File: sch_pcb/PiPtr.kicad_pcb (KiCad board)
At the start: 4 copper layers, 105 x 141.9 mm, 327 parts, among them J101 GLOBAL LINK 1 LEFT, J102 GLOBAL LINK 1 RIGHT, J104 GLOBAL LINK 2 LEFT, J106 GLOBAL LINK 2 RIGHT, J107 RASPBERRY_PI, J111 FP_PIXEL, J112 AM2302, J113 I2C1_5V, J114 I2C0_3v3, J117 OLED, J201 TO_SOUNDCARD, J202 FROM_SOUNDCARD, J203 Radio Port, J204 DB9_FEMALE, J301 SPARE, J302 SPARE, J303 SPARE, J304 SPARE, J305 USER_GPIO_2, J306 SPARE, J307 SPARE, J308 USER_GPIO_1, J309 SPARE, J310 SPARE, J311 USER_ADC, J313 SPARE, J314 SPARE, J315 12VDC_IN, J401 TO_SOUNDCARD, J402 FROM_SOUNDCARD, J403 Radio Port, J404 DB9_FEMALE, Q101 2N7000, Q102 2N7000, Q103 2N7000, Q104 2N7000, Q105 2N7000, Q201 2N7000, Q202 2N7000, Q203 2N7000, Q301 SPARE, Q302 SPARE, Q401 2N7000, Q402 2N7000, Q403 2N7000, U101 MCP23017, U102 IP4234CZ6, U103 MCP4351, U104 74HC138, U105 74LV1T125, U106 MCP4351, U107 MCP4351, U108 IP4234CZ6, U109 IP4234CZ6, U110 CD4050B, U111 74LV1T125, U112 74LV1T125, U201 MCP6004N, U202 74LVC1G3157, U203 74LVC1G3157, U204 74LVC4066, U205 MCP6004N, U206 74LVC1G3157, U207 MCP6S26, U301 MCP23017, U302 SPARE, U303 SPARE, U304 MCP3008, U305 MCP1703A-2502/MB, U306 TPS54302, U401 MCP6004N, U402 74LVC1G3157, U403 74LVC1G3157, U404 74LVC4066, U405 MCP6004N, U406 74LVC1G3157, U407 MCP6S26

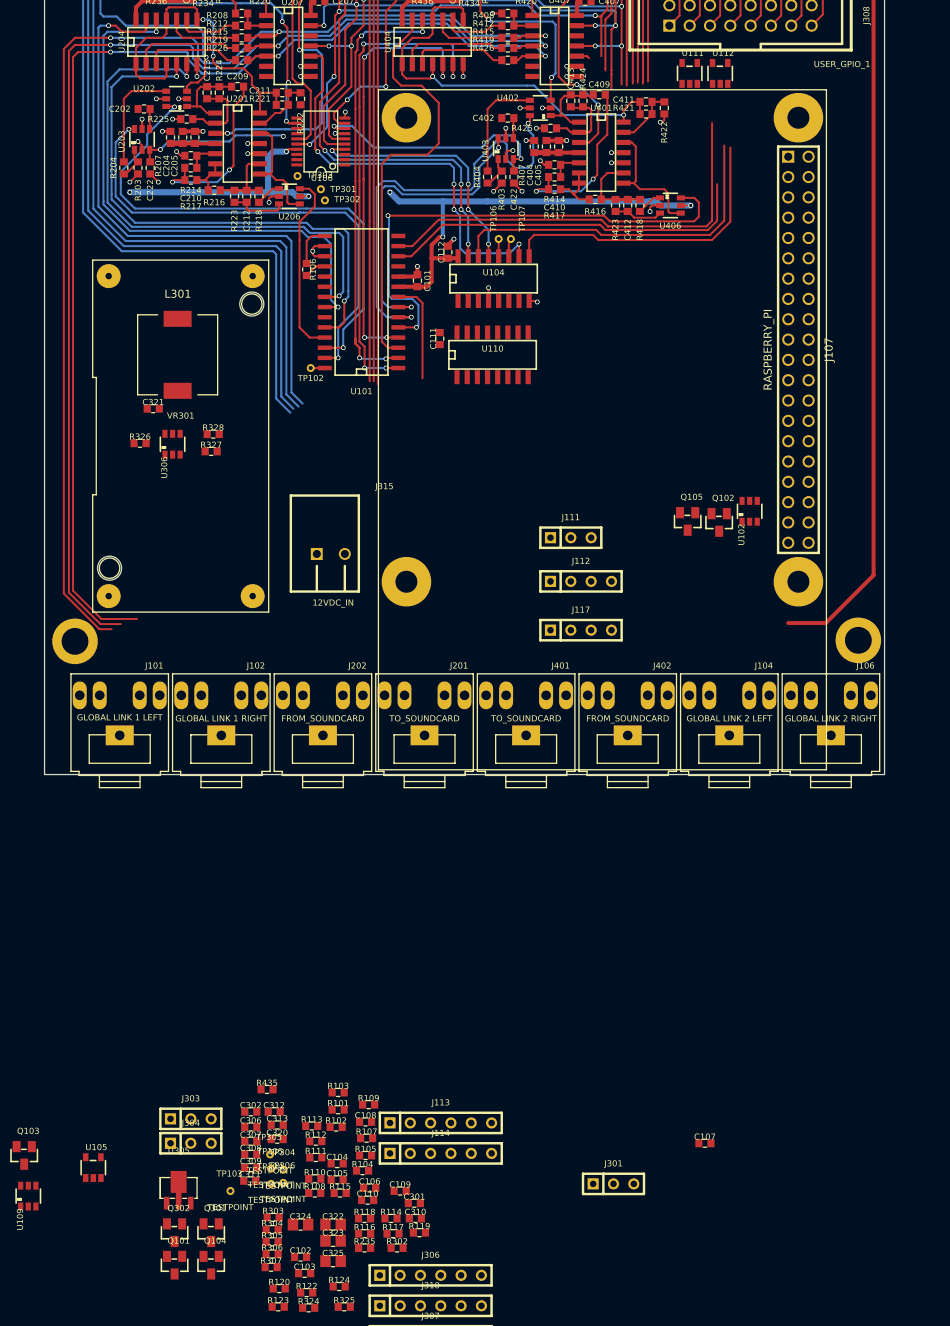
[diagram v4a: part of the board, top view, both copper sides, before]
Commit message: Add files via upload
Change link connectors to use a daughterboard for the off-rack links and 100mil headers for between-board links
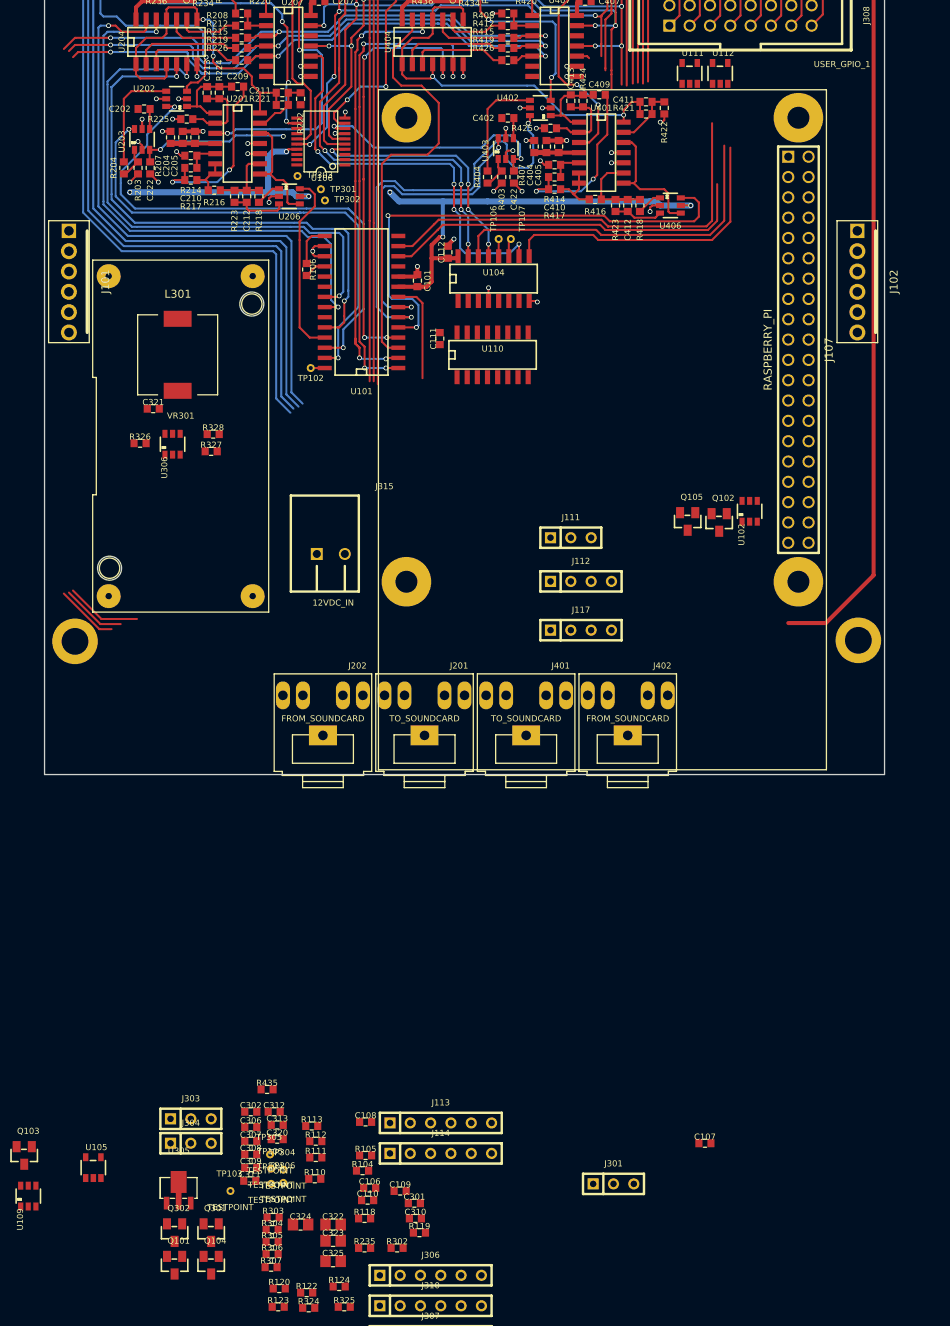
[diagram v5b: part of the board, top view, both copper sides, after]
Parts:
- removed C102, C104: 4.7u, lib:smd0603
- removed C103, C105: 0.1u, lib:smd0603
- removed J104: GLOBAL LINK 2 LEFT, lib:TRS3.5_5
- removed J106: GLOBAL LINK 2 RIGHT, lib:TRS3.5_5
- removed R101, R108: 100, lib:smd0603
- removed R102, R103, R107, R109, R114, R115, R116, R117: 2k, lib:smd0603
- C202, C402: value 4.7u -> 10u
- J101: value GLOBAL LINK 1 LEFT -> GLOBAL_LINK_LEFT; footprint lib:TRS3.5_5 -> lib:Molex_22-27-2061_100mil_6pin_verical
- J102: value GLOBAL LINK 1 RIGHT -> GLOBAL_LINK_RIGHT; footprint lib:TRS3.5_5 -> lib:Molex_22-27-2061_100mil_6pin_verical
- moved J102 96.7 mm to (158.8, 108.2), turned to 270 degrees
- moved J101 55.5 mm to (60.2, 108.2), turned to 270 degrees
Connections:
- J101 pad 1: GND -> +3V3
- J101 pad 2: /LINK1C -> /LINK1_AUD
- J101 pad 3: /LINK1_AUD -> /LINK1C
- J101 pad 4: Net-(J101-Pad4) -> GND
- J101 pad 5: Net-(J101-Pad5) -> /LINK2_AUD
- J102 pad 1: GND -> +3V3
- J102 pad 2: /LINK1C -> /LINK1_AUD
- J102 pad 3: /LINK1_AUD -> /LINK1C
- J102 pad 4: Net-(J102-Pad4) -> GND
- J102 pad 5: Net-(J102-Pad5) -> /LINK2_AUD
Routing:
- net /LINK2_AUD: track 150.2 -> 74.1 mm
- net /CH1/LOCAL_LINK: track 150.8 -> 82.7 mm
- net /LINK1_AUD: track 149.5 -> 81.8 mm
- net (no net): track 0.00 -> 9.47 mm

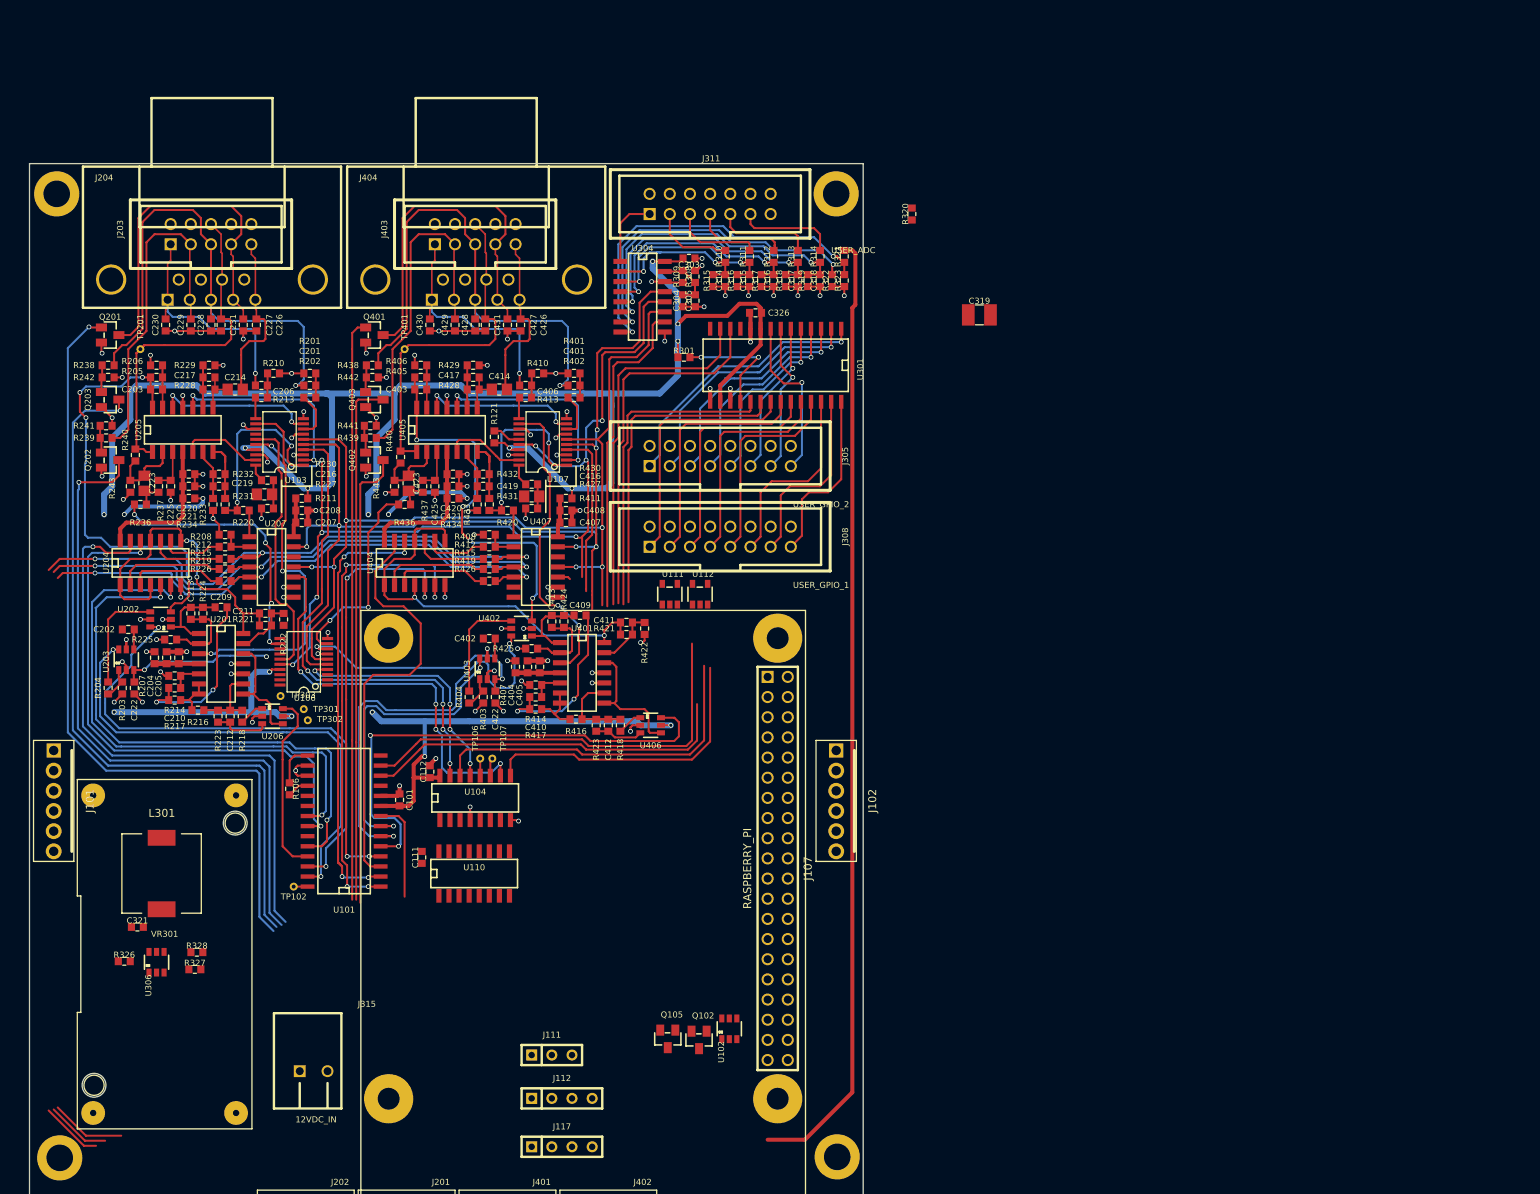
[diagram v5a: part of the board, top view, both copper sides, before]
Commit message: Add soundcard schematic
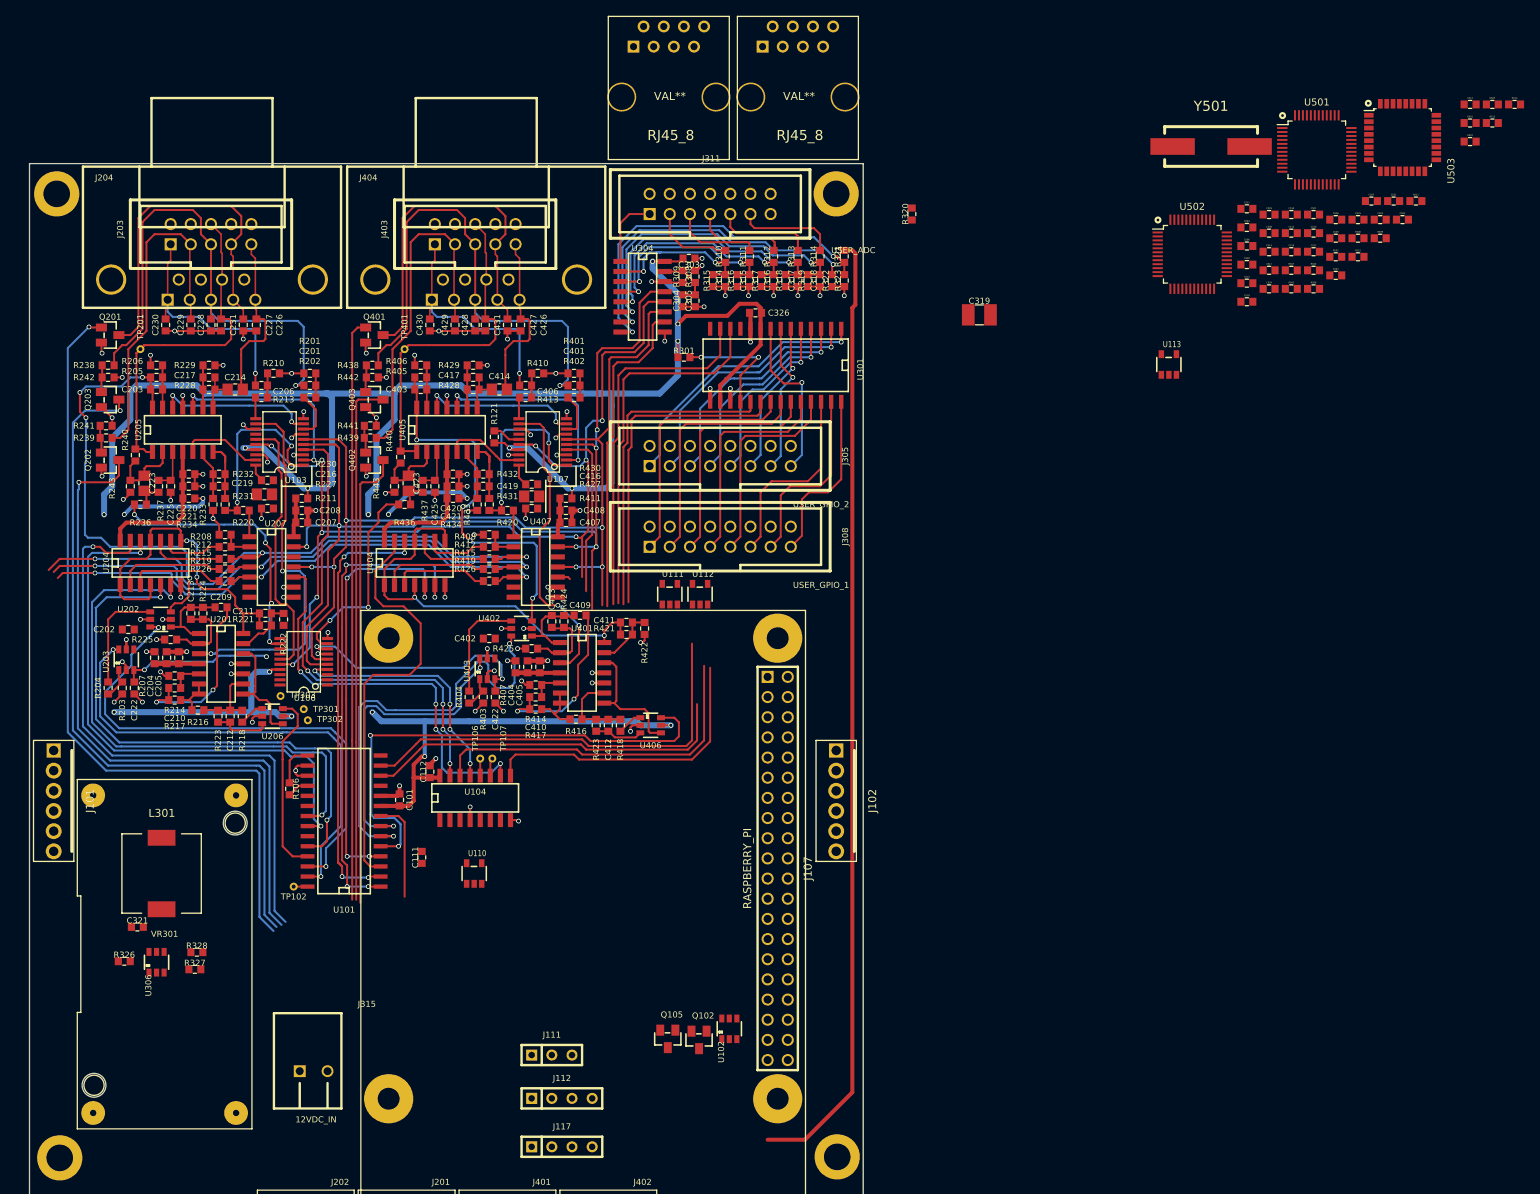
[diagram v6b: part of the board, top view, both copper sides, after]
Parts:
- added C501: 4u7, lib:smd0603, F.Cu at (218.9, 34.4)
- added C502: 100n, lib:smd0603, F.Cu at (230.1, 35.0)
- added C503: 4u7, lib:smd0603, F.Cu at (227.3, 35.0)
- added C504: 100n, lib:smd0603, F.Cu at (210.5, 36.0)
- added C505: 4u7, lib:smd0603, F.Cu at (213.3, 34.4)
- added C506: 100n, lib:smd0603, F.Cu at (210.5, 38.3)
- added C507: 4u7, lib:smd0603, F.Cu at (226.2, 32.7)
- added C508: 100n, lib:smd0603, F.Cu at (213.3, 36.7)
- added C509: 10u, lib:smd0603, F.Cu at (210.5, 40.7)
- added C510: 10u, lib:smd0603, F.Cu at (216.1, 34.4)
- added C511: 10u, lib:smd0603, F.Cu at (210.5, 33.6)
- added C512: 10u, lib:smd0603, F.Cu at (238.6, 20.5)
- added C513: 4u7, lib:smd0603, F.Cu at (216.1, 36.7)
- added C514: 4u7, lib:smd0603, F.Cu at (213.3, 39.0)
- added C515: 4u7, lib:smd0603, F.Cu at (210.5, 43.0)
- added C516: 4u7, lib:smd0603, F.Cu at (221.7, 35.0)
- added C517: 4u7, lib:smd0603, F.Cu at (213.3, 41.4)
- added C518: 4u7, lib:smd0603, F.Cu at (210.5, 45.3)
- added C519: 4u7, lib:smd0603, F.Cu at (216.1, 39.0)
- added C520: 4u7, lib:smd0603, F.Cu at (218.9, 36.7)
- added C521: 100n, lib:smd0603, F.Cu at (229.0, 32.7)
- added C522: 100n, lib:smd0603, F.Cu at (218.9, 39.0)
- added C523: 27p, lib:smd0603, F.Cu at (221.7, 42.0)
- added C524: 27p, lib:smd0603, F.Cu at (213.3, 43.7)
- added C525: 27p, lib:smd0603, F.Cu at (224.5, 35.0)
- added C526: 27p, lib:smd0603, F.Cu at (221.7, 37.3)
- added R501: 15k, lib:smd0603, F.Cu at (238.6, 22.8)
- added R502: 1k5, lib:smd0603, F.Cu at (221.7, 39.7)
- added R503: 22R, lib:smd0603, F.Cu at (216.1, 43.7)
- added R504: 22R, lib:smd0603, F.Cu at (218.9, 41.4)
- added R505: 22R, lib:smd0603, F.Cu at (241.4, 20.5)
- added R506: 22R, lib:smd0603, F.Cu at (224.5, 37.3)
- added R507: 22R, lib:smd0603, F.Cu at (216.1, 41.4)
- added R508: 22R, lib:smd0603, F.Cu at (218.9, 43.7)
- added R509: 15k, lib:smd0603, F.Cu at (227.3, 37.3)
- added R510: 15k, lib:smd0603, F.Cu at (238.6, 25.2)
- added R511: 15k, lib:smd0603, F.Cu at (231.8, 32.7)
- added R512: 15k, lib:smd0603, F.Cu at (224.5, 39.7)
- added R513: 15k, lib:smd0603, F.Cu at (241.4, 22.8)
- added R514: 1k5, lib:smd0603, F.Cu at (244.2, 20.5)
- added RJ45_8: VAL**, connect:RJ45_8, F.Cu at (137.7, 19.6)
- added RJ45_8: VAL**, connect:RJ45_8, F.Cu at (153.9, 19.6)
- added U113: 74LV1T125, lib:SOT23-5, F.Cu at (200.6, 53.2)
- added U501: CM108B, lib:LQFP-48_7x7mm_Pitch0.5mm, F.Cu at (219.3, 26.2)
- added U502: CM108B, lib:LQFP-48_7x7mm_Pitch0.5mm, F.Cu at (203.6, 39.4)
- added U503: TUSB2036, lib:LQFP-32_7x7mm_Pitch0.8mm, F.Cu at (230.1, 24.7)
- added Y501: 6MHz, lib:Crystal_HC49-SD_SMD, F.Cu at (206.0, 25.8)
- J117: value OLED -> OLED_SSD1306
- U104: value 74HC138 -> 74HCT138
- U110: value CD4050B -> 74LV1T125; footprint lib:SOIC16 -> lib:SOT23-5
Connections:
- C111 pad 1: GND -> +5V
- C111 pad 2: +5V -> GND
- C202 pad 2: Net-(C202-Pad2) -> (no net)
- C216 pad 1: Net-(C216-Pad1) -> (no net)
- C402 pad 2: Net-(C402-Pad2) -> (no net)
- C416 pad 1: Net-(C416-Pad1) -> (no net)
- J112 pad 3: (no net) -> Net-(J112-Pad3)
- J203 pad 10: (no net) -> Net-(J203-Pad10)
- J307 pad 1: (no net) -> Net-(J307-Pad1)
- J311 pad 13: (no net) -> Net-(J311-Pad13)
- J403 pad 10: (no net) -> Net-(J403-Pad10)
- MTG301 pad 1: (no net) -> Net-(MTG301-Pad1)
- MTG302 pad 1: (no net) -> Net-(MTG302-Pad1)
- MTG303 pad 1: (no net) -> Net-(MTG303-Pad1)
- MTG304 pad 1: (no net) -> Net-(MTG304-Pad1)
- R227 pad 2: Net-(C216-Pad1) -> /CH1/FROM_SOUNDCARD
- R230 pad 2: Net-(C216-Pad1) -> /CH1/FROM_SOUNDCARD
- R427 pad 2: Net-(C416-Pad1) -> /CH2/FROM_SOUNDCARD
- R430 pad 2: Net-(C416-Pad1) -> /CH2/FROM_SOUNDCARD
- U101 pad 19: (no net) -> Net-(U101-Pad19)
- U101 pad 20: (no net) -> Net-(U101-Pad20)
- U104 pad 1: Net-(U104-Pad1) -> /SELA_33
- U104 pad 2: Net-(U104-Pad2) -> /SELB_33
- U104 pad 3: Net-(U104-Pad3) -> /SELC_33
- U104 pad 5: Net-(U104-Pad5) -> /CE0_33
- U110 pad 1: +5V -> GND
- U110 pad 2: Net-(U104-Pad1) -> /SCLK_33
- U110 pad 3: /SELA_33 -> GND
- U110 pad 4: Net-(U104-Pad2) -> SCLK_5
- U110 pad 5: /SELB_33 -> +5V
- U203 pad 4: Net-(C202-Pad2) -> /CH1/TO_SOUNDCARD
- U207 pad 12: (no net) -> Net-(U207-Pad12)
- U207 pad 6: (no net) -> Net-(U207-Pad6)
- U207 pad 7: (no net) -> Net-(U207-Pad7)
- U403 pad 4: Net-(C402-Pad2) -> /CH2/TO_SOUNDCARD
- U407 pad 12: (no net) -> Net-(U407-Pad12)
- U407 pad 6: (no net) -> Net-(U407-Pad6)
- U407 pad 7: (no net) -> Net-(U407-Pad7)
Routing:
- net +5V: track 431.3 -> 409.8 mm
- net (no net): track 9.47 -> 0.00 mm
- net /LINK1_AUD: track 81.8 -> 73.7 mm
- net /CH1/LOCAL_LINK: track 82.7 -> 74.9 mm
- net Net-(C216-Pad1): track 3.38 -> 0.00 mm
- net Net-(C416-Pad1): track 3.05 -> 0.00 mm
- net Net-(C402-Pad2): track 2.53 -> 0.00 mm
- net Net-(C202-Pad2): track 2.53 -> 0.00 mm
